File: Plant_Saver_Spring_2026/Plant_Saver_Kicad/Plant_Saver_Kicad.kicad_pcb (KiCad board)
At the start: 2 copper layers, 80.5 x 83 mm, 113 parts, among them J10 1.25mm, J11 DM3D-SF, J2 SBH11-PBPC-D05-ST-BK, J3 Test, J4 SM04B-SRSS-TB, J6 Conn_01x02_Pin, J7 Conn_01x06_Socket, J8 S3B-PH-K-S, J9 54-00284, Q1 G09P02L, Q10 G09P02L, Q11 ISP12DP06NMXTSA1, Q12 G09P02L, Q2 G09P02L, Q3 ISP12DP06NMXTSA1, Q4 G09P02L, Q5 G09P02L, Q6 G09P02L, Q7 G09P02L, Q8 G09P02L, Q9 G09P02L, SW1 Reset, SW2 1101M2S3AQE2, SW3 Boot, SW4 SA72SB0, U1 CDBA140SL-HF, U10 DW03C, U11 CDBA140SL-HF, U12 LP38511TJ-ADJ/NOPB, U13 MCP73833-xxx-UN, U14 MCP6234, U15 MCP73833-xxx-UN, U16 MCP6547T_I_MS, U2 CDBA140SL-HF, U3 CDBA140SL-HF, U4 CDBA140SL-HF, U5 ESP32-WROOM-32E-N16, U9 CDBA140SL-HF

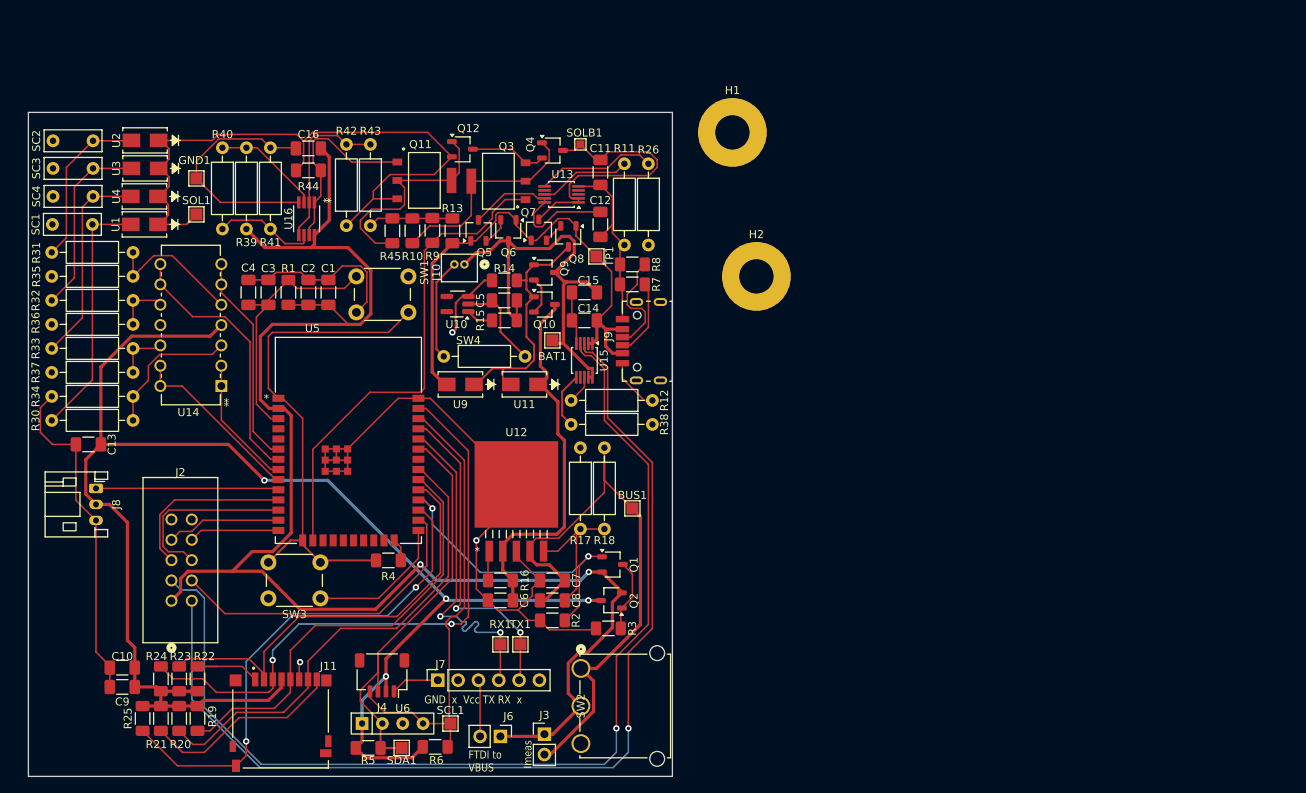
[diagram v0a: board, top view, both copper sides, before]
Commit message: Further PCB Improvements
Finally fixed STAT1 STAT2 running along bottom of board.
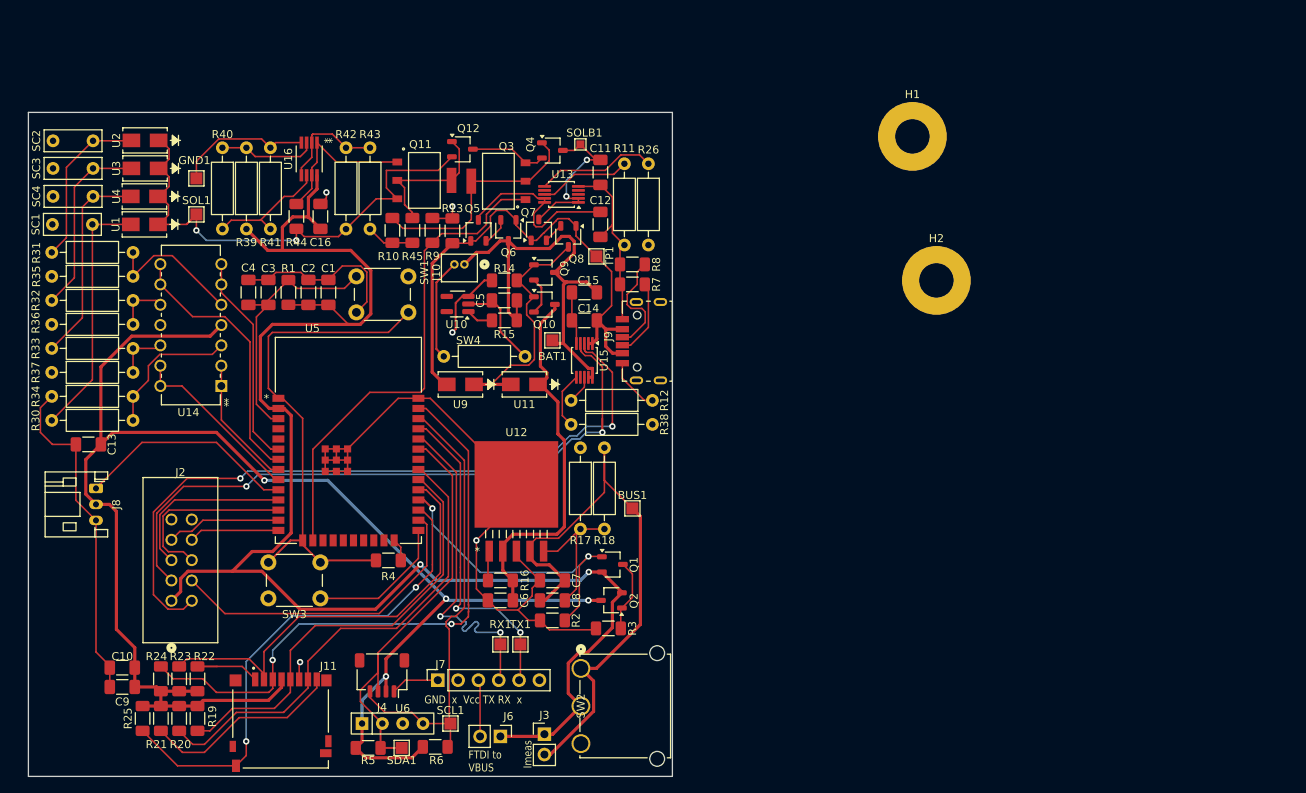
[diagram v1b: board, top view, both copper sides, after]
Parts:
- moved H1 22.5 mm to (137.5, 70.5)
- moved H2 22.5 mm to (140.5, 88.5)
- moved C16 8.63 mm to (63.5, 80.5), turned to 90 degrees
- moved U16 7.48 mm to (62.1, 73.3)
- moved R44 5.94 mm to (60.5, 80.5), turned to 90 degrees
- moved R10 2.50 mm to (72.5, 82.2), turned to -90 degrees
- moved R45 2.50 mm to (75.0, 82.2), turned to 90 degrees
- moved R42 0.42 mm to (66.7, 82.1)
- moved R43 0.42 mm to (69.7, 71.9)
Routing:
- net STAT2: track 130.5 -> 83.5 mm, vias 1 -> 2
- net STAT1: track 127.5 -> 90.8 mm, vias 1 -> 2
- net /Power_And_Charging/Solar: track 83.9 -> 65.0 mm, vias 0 -> 2
- net /Power_And_Charging/MCP73833_Solar/Vin: track 35.6 -> 21.1 mm, vias 0 -> 2
- net GND: track 308.1 -> 296.2 mm, vias 3 -> 5
- net Net-(Q11-D): track 27.9 -> 17.9 mm
- net Net-(U16A--): track 20.8 -> 13.6 mm
- net Net-(Q11-G): track 24.6 -> 19.8 mm
- net Aout: track 22.9 -> 27.6 mm
- net Net-(U16B--): track 12.9 -> 15.6 mm
- net Net-(Q3-D): track 26.5 -> 29.1 mm
- net Net-(U16A-+): track 13.6 -> 12.3 mm
- net Vperiph: track 196.2 -> 197.4 mm
- net Vbus: track 192.3 -> 193.0 mm
- net Net-(Q10-G): track 31.5 -> 31.0 mm
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
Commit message: PCB Adjustments
Placed Mounting holes and attributions, cleaned up some traces. Still needs ground plane behind.
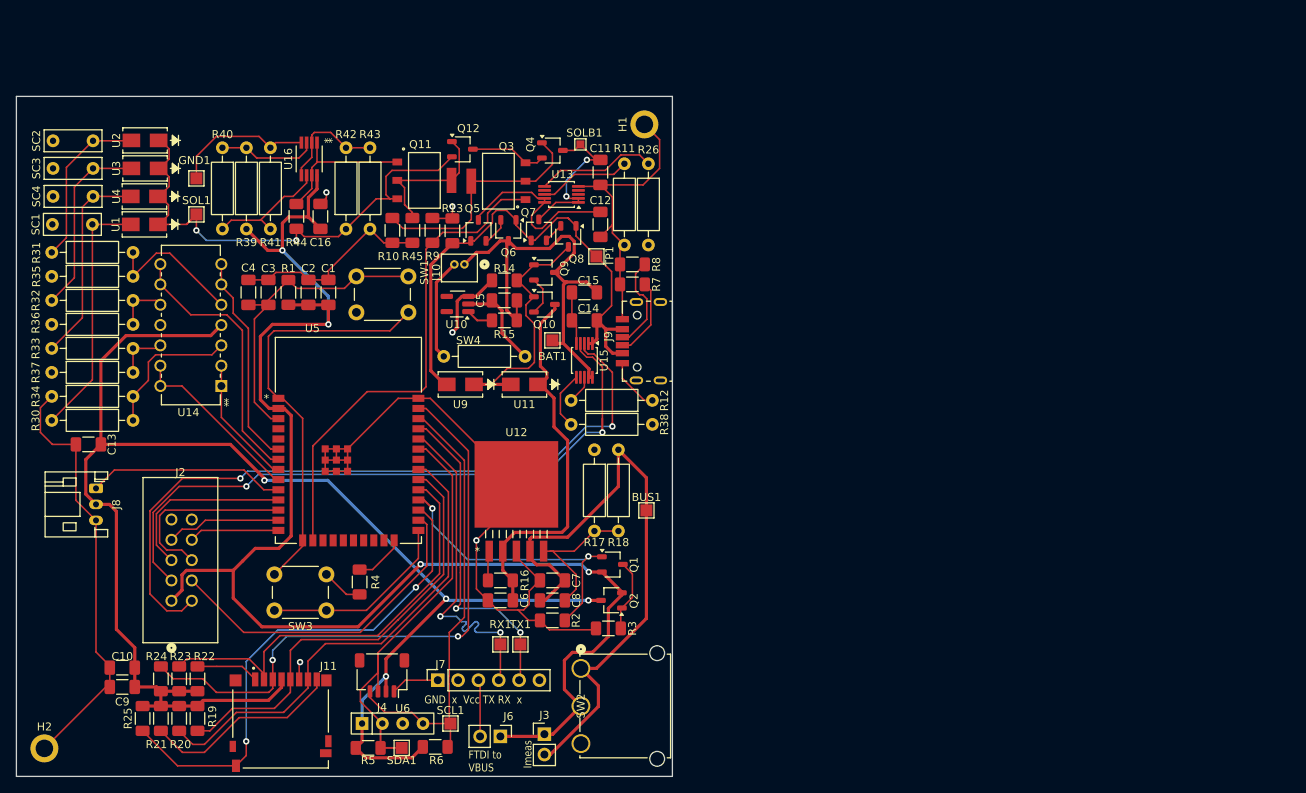
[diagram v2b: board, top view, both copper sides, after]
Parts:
- H1, H2: footprint MountingHole:MountingHole_4.3mm_M4_Pad -> MountingHole:MountingHole_2.2mm_M2_ISO7380_Pad
- moved H2 125.9 mm to (29.0, 147.0)
- moved H1 33.5 mm to (104.0, 69.0), turned to 90 degrees
- moved R4 4.50 mm to (68.4, 126.2), turned to 90 degrees
- moved BUS1 1.77 mm to (104.2, 117.2)
- moved R17 1.77 mm to (97.8, 109.7)
- moved R18 1.77 mm to (100.8, 119.8)
- moved SW3 1.68 mm to (64.2, 129.8)
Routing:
- net GND: track 296.2 -> 315.5 mm
- net Vbus: track 193.0 -> 185.2 mm, vias 2 -> 4
- net Net-(U5-EN): track 32.7 -> 39.4 mm
- net Net-(U5-IO0): track 17.8 -> 24.2 mm
- net Net-(U5-IO2): track 2.85 -> 6.38 mm
- net Aout: track 27.6 -> 24.8 mm
- net Error: track 40.0 -> 42.0 mm
- net /Power_And_Charging/Vout: track 77.1 -> 78.7 mm
- net Net-(J9-CC2): track 13.5 -> 12.1 mm
- net Periph_EN: track 37.9 -> 36.6 mm
- net STAT1: track 90.8 -> 92.0 mm
- net Net-(Q11-G): track 19.8 -> 18.8 mm
- net SPI_MOSI: track 76.0 -> 76.9 mm
- net Net-(Q3-D): track 29.1 -> 29.9 mm
- net /Power_And_Charging/Solar: track 65.0 -> 64.2 mm
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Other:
- board size 80.5 x 83 mm -> 82 x 85 mm
- board text added: "Brandon Early Donovan Ghysels Noah Schmidt Sebastian Stauber Jackson Wiles"
- board text added: "MTU Open Source Hardware Enterprise oshe.io"

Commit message: PCB Finishing Steps
Added additional details on silkscreen, added ground plane, misc. touchups
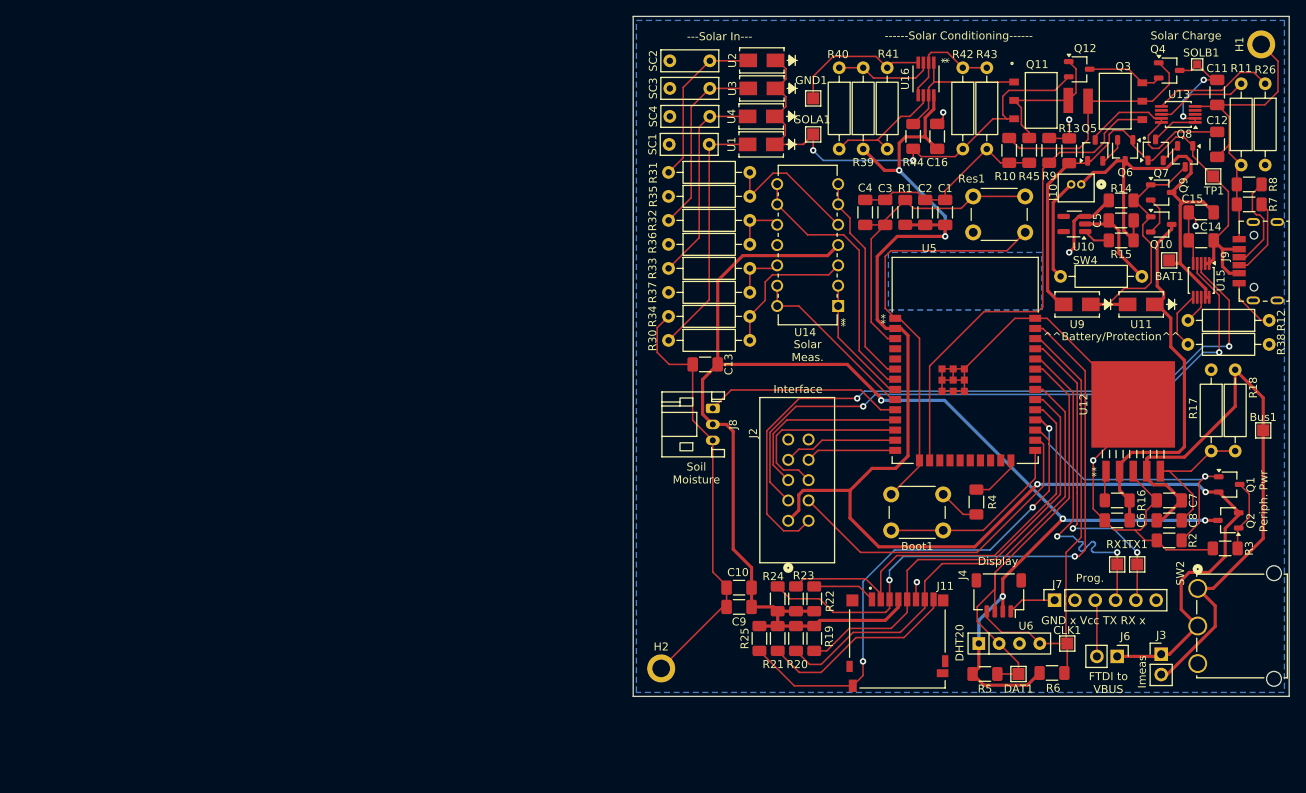
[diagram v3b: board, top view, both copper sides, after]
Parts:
- added REF**: OSHW-Symbol_6.7x6mm_SilkScreen, Symbol:OSHW-Symbol_6.7x6mm_SilkScreen, B.Cu at (111.0, 118.6)
- moved SW2 77.7 mm to (173.2, 127.0)
- moved J4 77.7 mm to (148.3, 127.9)
- moved J7 77.7 mm to (155.3, 128.5)
- moved Q7 77.7 mm to (167.9, 72.2)
- moved R42 77.7 mm to (143.8, 72.1)
- moved R43 77.7 mm to (146.8, 61.9)
- moved SC2 77.7 mm to (112.2, 61.0)
- moved SC3 77.7 mm to (112.2, 64.5)
- moved SC4 77.7 mm to (112.2, 68.0)
- moved SW4 77.7 mm to (166.2, 88.0)
- moved U13 77.7 mm to (170.7, 67.8)
- moved U2 77.7 mm to (118.7, 61.0)
- moved U3 77.7 mm to (118.7, 64.5)
- moved BAT1 77.7 mm to (169.6, 86.0)
- moved Boot1 77.7 mm to (141.3, 119.8)
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- renumbered SW3 to Boot1, BUS1 to Bus1, SCL1 to CLK1, SDA1 to DAT1, SW1 to Res1, SOL1 to SOLA1
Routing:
- net GND: track 315.5 -> 318.9 mm, vias 5 -> 6
- net STAT2: track 84.2 -> 82.0 mm
- net SDA: track 53.5 -> 55.5 mm
- net Vbus: track 185.2 -> 183.6 mm
- net Vperiph: track 196.8 -> 197.7 mm
- net SCL: track 57.4 -> 58.2 mm
- added copper zone on B.Cu, net GND
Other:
- board text added: "------Solar Conditioning------"
- board text added: "---Solar In---"
- board text added: "DHT20"
- board text added: "Display"
- board text added: "Interface"
- board text added: "Periph. Pwr"
- board text added: "Plant-Saver"
- board text added: "Prog."
- board text added: "Soil Moisture"
- board text added: "Solar Charge"
- board text added: "Solar Meas."
- board text added: "^^Battery/Protection^^"

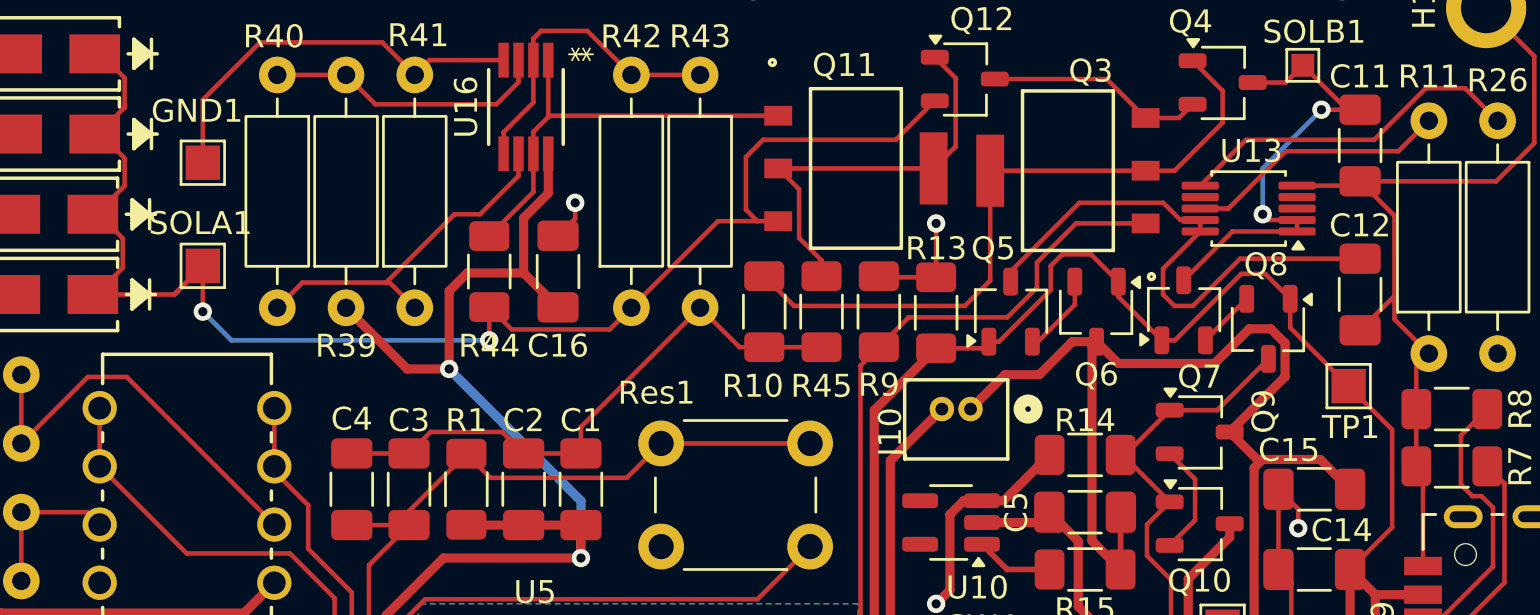
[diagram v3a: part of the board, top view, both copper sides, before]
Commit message: Finalizing checks/tweaks to PCB
Fixed a few footprint mask and silkscreen issues
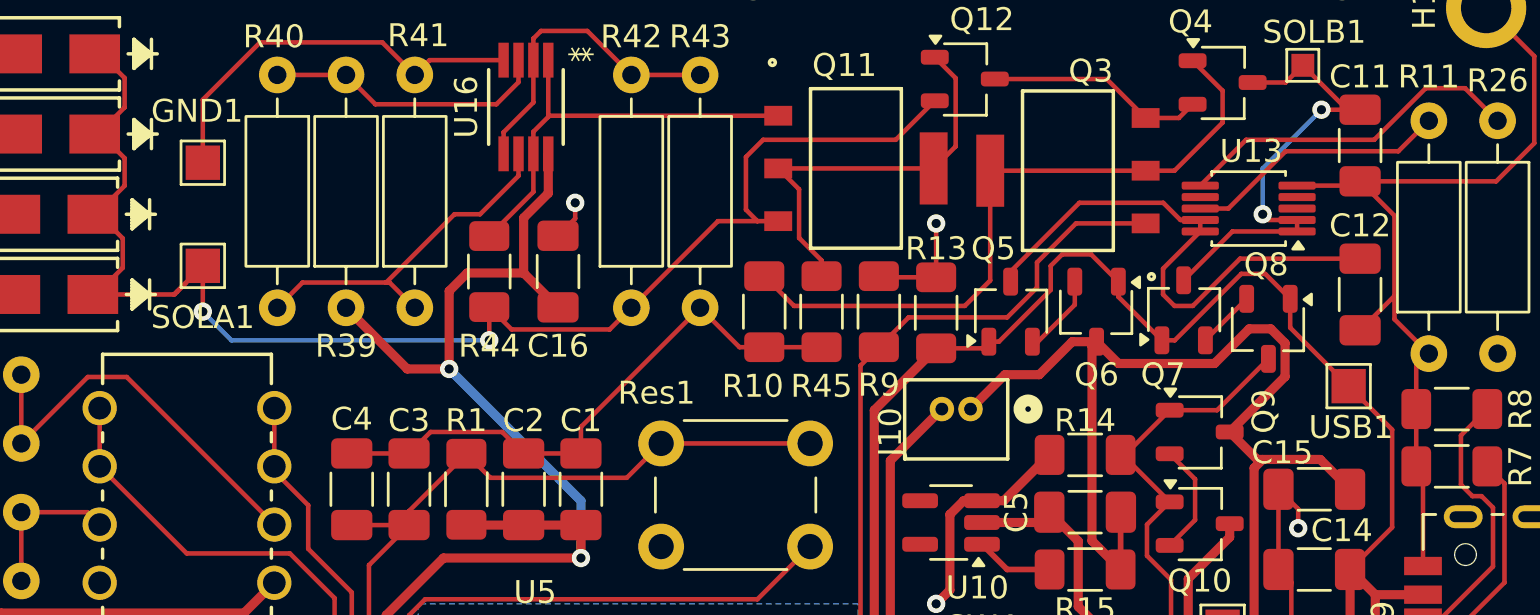
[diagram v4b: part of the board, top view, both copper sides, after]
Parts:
- renumbered TP1 to USB1
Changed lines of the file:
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@@
 		(tags "TSOT-23")
 		(property "Reference" "Q7"
-			(at -2.91 0.7 180)
+			(at -2.81 -0.9 180)
 			(layer "F.SilkS")
 			(effects
@@
 		(descr "SMD rectangular pad as test Point, square 1.5mm side length")
 		(tags "test point SMD pad rectangle square")
-		(property "Reference" "TP1"
+		(property "Reference" "USB1"
 			(at 1.8 -0.1 180)
 			(layer "F.SilkS")
@@
 		(tags "capacitor handsolder")
 		(property "Reference" "C15"
-			(at 1.1 1.7 0)
+			(at 1.4 1.6 0)
 			(layer "F.SilkS")
 			(effects
@@
 			(pinfunction "CC1")
 			(pintype "bidirectional")
-			(solder_mask_margin 0.102)
+			(solder_mask_margin 0.08)
 		)
 		(pad "A9" smd rect
@@
 			(pinfunction "VBUS_A")
 			(pintype "power_in")
-			(solder_mask_margin 0.102)
+			(solder_mask_margin 0.08)
 		)
 		(pad "A12" smd rect
@@
 			(pinfunction "CC2")
 			(pintype "bidirectional")
-			(solder_mask_margin 0.102)
+			(solder_mask_margin 0.08)
 		)
 		(pad "B9" smd rect
@@
 			(pinfunction "VBUS_B")
 			(pintype "power_in")
-			(solder_mask_margin 0.102)
+			(solder_mask_margin 0.08)
 		)
 		(pad "B12" smd rect
@@
 		(sheetname "/MicroSD/")
 		(sheetfile "MicroSD.kicad_sch")
-		(clearance 0.15)
 		(attr smd)
 		(fp_line
@@
 			(pinfunction "DAT1")
 			(pintype "bidirectional")
-			(solder_mask_margin 0.102)
+			(solder_mask_margin 0.075)
 		)
 		(pad "S1" smd rect
@@
 			(pinfunction "SHIELD")
 			(pintype "passive+no_connect")
-			(solder_mask_margin 0.102)
+			(solder_mask_margin 0.075)
 		)
 		(pad "S2" smd rect
@@
 		(tags "test point SMD pad rectangle square")
 		(property "Reference" "SOLA1"
-			(at -0.1 -1.85 0)
+			(at 0 2.25 0)
 			(layer "F.SilkS")
 			(effects
@@
 		)
 	)
+	(dimension
+		(type orthogonal)
+		(layer "Dwgs.User")
+		(pts
+			(xy 106.1 137) (xy 106.1 140.5)
+		)
+		(height -5.9)
+		(orientation 1)
+		(format
+			(prefix "")
+			(suffix "")
+			(units 3)
+			(units_format 0)
+			(precision 4)
+			(suppress_zeroes yes)
+		)
+		(style
+			(thickness 0.15)
+			(arrow_length 1.27)
+			(text_position_mode 0)
+			(arrow_direction outward)
+			(extension_height 0.58642)
+			(extension_offset 0.5)
+			(keep_text_aligned yes)
+		)
+		(gr_text "3.5"
+			(at 99.05 138.75 90)
+			(layer "Dwgs.User")
+			(effects
+				(font
+					(size 1 1)
+					(thickness 0.15)
+				)
+			)
+		)
+	)
+	(dimension
+		(type orthogonal)
+		(layer "Dwgs.User")
+		(pts
+			(xy 106.1 137) (xy 102.6 137)
+		)
+		(height 6.9)
+		(orientation 0)
+		(format
+			(prefix "")
+			(suffix "")
+			(units 3)
+			(units_format 0)
+			(precision 4)
+			(suppress_zeroes yes)
+		)
+		(style
+			(thickness 0.15)
+			(arrow_length 1.27)
+			(text_position_mode 0)
+			(arrow_direction outward)
+			(extension_height 0.58642)
+			(extension_offset 0.5)
+			(keep_text_aligned yes)
+		)
+		(gr_text "3.5"
+			(at 104.35 142.75 0)
+			(layer "Dwgs.User")
+			(effects
+				(font
+					(size 1 1)
+					(thickness 0.15)
+				)
+			)
+		)
+	)
+	(dimension
+		(type orthogonal)
+		(layer "Dwgs.User")
+		(pts
+			(xy 184.6 55.5) (xy 102.6 55.5)
+		)
+		(height -1.9)
+		(orientation 0)
+		(format
+			(prefix "")
+			(suffix "")
+			(units 3)
+			(units_format 0)
+			(precision 4)
+			(suppress_zeroes yes)
+		)
+		(style
+			(thickness 0.15)
+			(arrow_length 1.27)
+			(text_position_mode 0)
+			(arrow_direction outward)
+			(extension_height 0.58642)
+			(extension_offset 0.5)
+			(keep_text_aligned yes)
+		)
+		(gr_text "82"
+			(at 143.6 52.45 0)
+			(layer "Dwgs.User")
+			(effects
+				(font
+					(size 1 1)
+					(thickness 0.15)
+				)
+			)
+		)
+	)
+	(dimension
+		(type orthogonal)
+		(layer "Dwgs.User")
+		(pts
+			(xy 184.6 55.5) (xy 184.6 140.5)
+		)
+		(height 2.9)
+		(orientation 1)
+		(format
+			(prefix "")
+			(suffix "")
+			(units 3)
+			(units_format 0)
+			(precision 4)
+			(suppress_zeroes yes)
+		)
+		(style
+			(thickness 0.15)
+			(arrow_length 1.27)
+			(text_position_mode 0)
+			(arrow_direction outward)
+			(extension_height 0.58642)
+			(extension_offset 0.5)
+			(keep_text_aligned yes)
+		)
+		(gr_text "85"
+			(at 186.35 98 90)
+			(layer "Dwgs.User")
+			(effects
+				(font
+					(size 1 1)
+					(thickness 0.15)
+				)
+			)
+		)
+	)
 	(segment
 		(start 136.6375 70.5625)
@@
 	)
 	(segment
-		(start 180.18 62.5)
-		(end 181.6 63.92)
+		(start 170.625 64.75)
+		(end 168.625 66.75)
 		(width 0.2)
 		(layer "F.Cu")
@@
 	)
 	(segment
-		(start 168.625 66.75)
-		(end 170.625 64.75)
+		(start 180.18 62.5)
+		(end 181.6 63.92)
 		(width 0.2)
 		(layer "F.Cu")
